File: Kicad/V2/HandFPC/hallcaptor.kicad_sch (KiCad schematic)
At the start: 0 parts

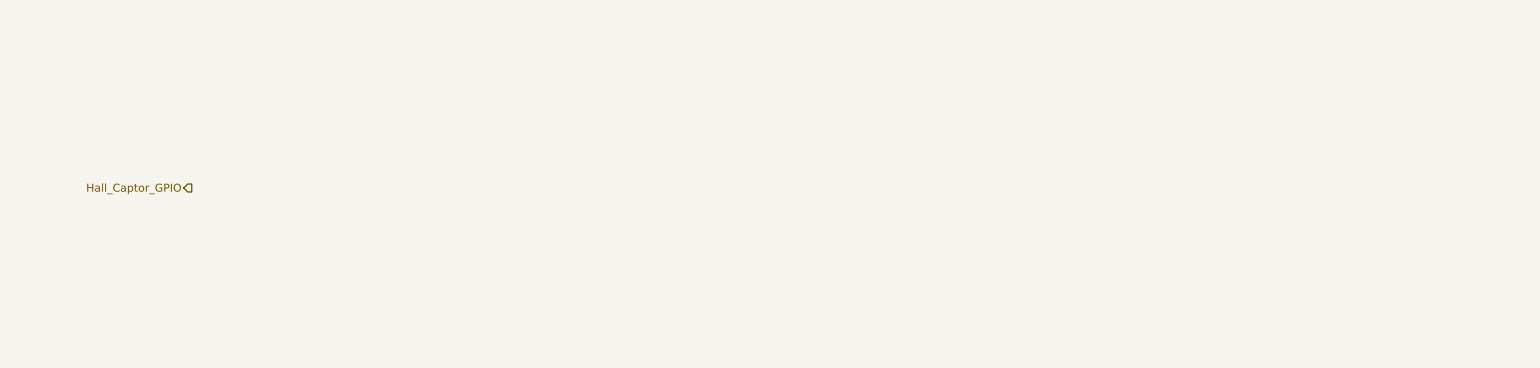
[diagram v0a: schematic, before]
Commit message: hand FPC pass erc no warning no error
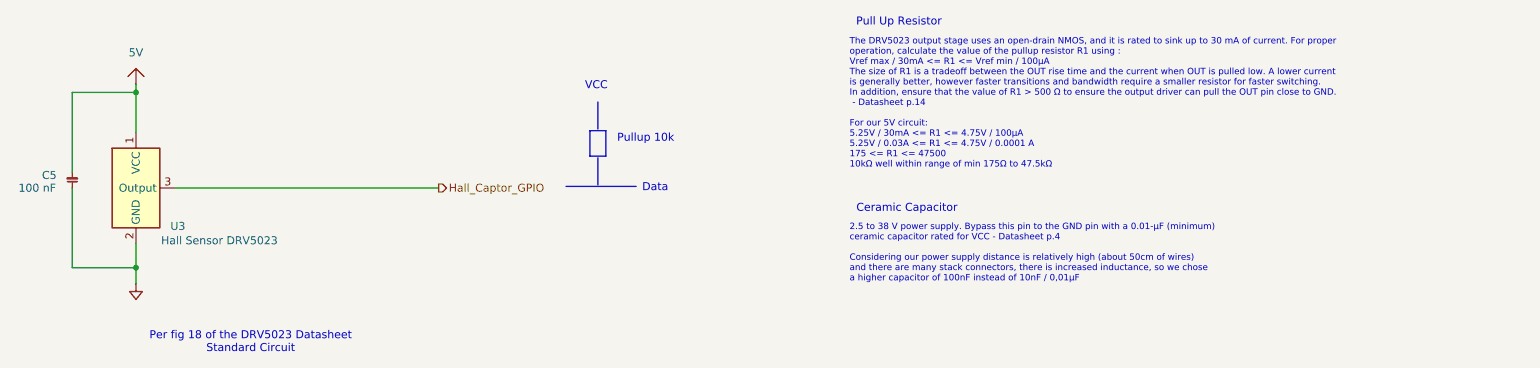
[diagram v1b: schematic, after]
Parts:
- added C5: 100 nF, symbol G-Love-Symbols:C
- added U3: Hall Sensor DRV5023, symbol G-Love-Symbols:DRV5023
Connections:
- net Hall_Captor_GPIO: now also U3.3 (Output)
- new net 5V: C5.1, U3.1 (VCC)
- new net GND: C5.2, U3.2 (GND)
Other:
- note added: "2.5 to 38 V power supply. Bypass this pin to the GND pin with a 0.01-μF (minimum) ceramic capacitor rated for VCC - Datasheet p.4 Considering our power supply distance is relatively high (about 50cm of wires) and there are many stack connectors, there is increased inductance, so we chose a higher capacitor of 100nF instead of 10nF / 0,01μF"
- note added: "Ceramic Capacitor"
- note added: "Data"
- note added: "Per fig 18 of the DRV5023 Datasheet Standard Circuit"
- note added: "Pull Up Resistor"
- note added: "Pullup 10k"
- note added: "The DRV5023 output stage uses an open-drain NMOS, and it is rated to sink up to 30 mA of current. For proper operation, calculate the value of the pullup resistor R1 using : Vref max / 30mA <= R1 <= Vref min / 100μA The size of R1 is a tradeoff between the OUT rise time and the current when OUT is pulled low. A lower current is generally better, however faster transitions and bandwidth require a 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"
- note added: "VCC"

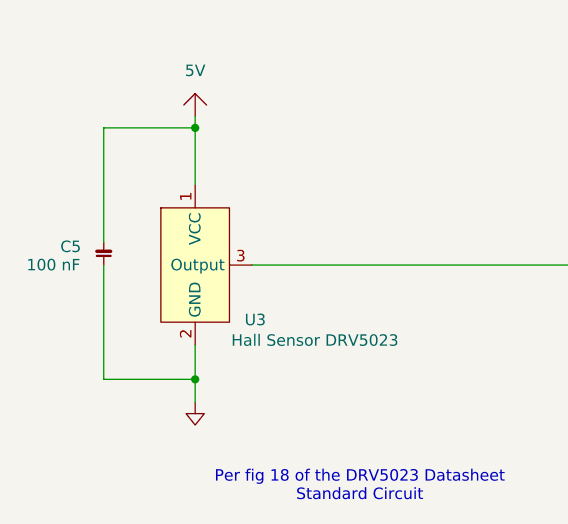
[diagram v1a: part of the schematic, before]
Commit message: add custom symbol for FPC connector
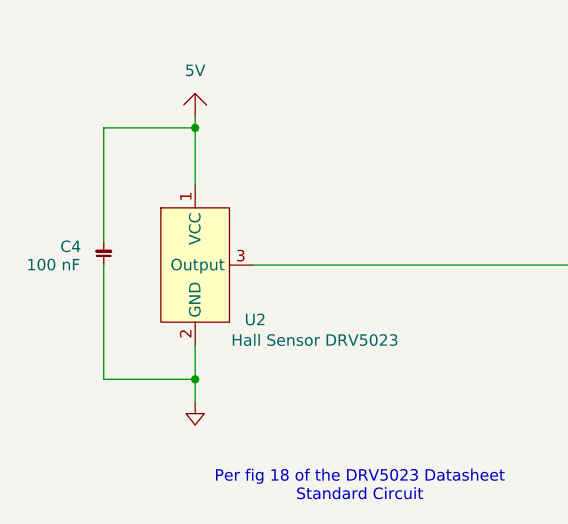
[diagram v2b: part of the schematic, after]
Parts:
- renumbered C5 to C4, U3 to U2
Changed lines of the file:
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@@
 		(dnp no)
 		(fields_autoplaced yes)
-		(property "Reference" "#PWR025"
+		(property "Reference" "#PWR024"
 			(at 50.8 27.3049 0)
 			(hide yes)
@@
 			(project "HandFPC"
 				(path "/7221f3d8-f3bc-4a50-a6fd-69c2d8ca27db/54aec40e-cdbe-47d9-8050-c74604c00f1a"
-					(reference "#PWR025")
+					(reference "#PWR024")
 					(unit 1)
 				)
@@
 		(in_pos_files yes)
 		(dnp no)
-		(property "Reference" "C5"
+		(property "Reference" "C4"
 			(at 33.274 44.958 0)
 			(show_name no)
@@
 			(project "HandFPC"
 				(path "/7221f3d8-f3bc-4a50-a6fd-69c2d8ca27db/54aec40e-cdbe-47d9-8050-c74604c00f1a"
-					(reference "C5")
+					(reference "C4")
 					(unit 1)
 				)
@@
 		(in_pos_files yes)
 		(dnp no)
-		(property "Reference" "U3"
+		(property "Reference" "U2"
 			(at 56.134 53.086 0)
 			(show_name no)
@@
 			(project "HandFPC"
 				(path "/7221f3d8-f3bc-4a50-a6fd-69c2d8ca27db/54aec40e-cdbe-47d9-8050-c74604c00f1a"
-					(reference "U3")
-					(unit 1)
-				)
+					(reference "U2")
+					(unit 1)
+				)

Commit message: fix flex sensor mixed up with force sensor
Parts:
- C4: footprint (none) -> MyGlove:Capacitor_0603
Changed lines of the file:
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@@
 			)
 		)
-		(property "Footprint" ""
+		(property "Footprint" "MyGlove:Capacitor_0603"
 			(at 38.1 45.72 0)
 			(hide yes)

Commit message: add FPC footprints
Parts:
- C4: footprint MyGlove:Capacitor_0603 -> MyGlove:FPC_0603
- U2: footprint (none) -> MyGlove:FPC_SOT_23
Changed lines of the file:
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@@
 			)
 		)
-		(property "Footprint" "MyGlove:Capacitor_0603"
+		(property "Footprint" "MyGlove:FPC_0603"
 			(at 38.1 45.72 0)
 			(hide yes)
@@
 			)
 		)
-		(property "Footprint" ""
+		(property "Footprint" "MyGlove:FPC_SOT_23"
 			(at 48.26 44.45 0)
 			(hide yes)

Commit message: add routing
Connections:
- net 5V renamed +3.3V
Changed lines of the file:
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@@
-	)
-	(symbol
-		(lib_id "G-Love-Symbols:+5V")
-		(at 48.26 27.94 0)
-		(unit 1)
-		(body_style 1)
-		(exclude_from_sim no)
-		(in_bom no)
-		(on_board no)
-		(in_pos_files yes)
-		(dnp no)
-		(fields_autoplaced yes)
-		(property "Reference" "#PWR024"
-			(at 50.8 27.3049 0)
-			(hide yes)
-			(show_name no)
-			(do_not_autoplace no)
-			(effects
-				(font
-					(size 1.27 1.27)
-				)
-				(justify left)
-			)
-		)
-		(property "Value" "5V"
-			(at 48.26 25.4 0)
-			(show_name no)
-			(do_not_autoplace no)
-			(effects
-				(font
-					(size 1.27 1.27)
-				)
-			)
-		)
-		(property "Footprint" ""
-			(at 48.26 27.94 0)
-			(hide yes)
-			(show_name no)
-			(do_not_autoplace no)
-			(effects
-				(font
-					(size 1.27 1.27)
-				)
-			)
-		)
-		(property "Datasheet" ""
-			(at 48.26 27.94 0)
-			(hide yes)
-			(show_name no)
-			(do_not_autoplace no)
-			(effects
-				(font
-					(size 1.27 1.27)
-				)
-			)
-		)
-		(property "Description" ""
-			(at 48.26 27.94 0)
-			(hide yes)
-			(show_name no)
-			(do_not_autoplace no)
-			(effects
-				(font
-					(size 1.27 1.27)
-				)
-			)
-		)
-		(pin "1"
-		)
-		(instances
-			(project "HandFPC"
-				(path "/7221f3d8-f3bc-4a50-a6fd-69c2d8ca27db/54aec40e-cdbe-47d9-8050-c74604c00f1a"
-					(reference "#PWR024")
-					(unit 1)
-				)
-			)
-		)
 	)
 	(symbol
@@
 					(unit 1)
 				)
+			)
+		)
+	)
+	(symbol
+		(lib_id "G-Love-Symbols:+3.3V")
+		(at 48.26 29.21 0)
+		(unit 1)
+		(body_style 1)
+		(exclude_from_sim no)
+		(in_bom no)
+		(on_board no)
+		(in_pos_files yes)
+		(dnp no)
+		(property "Reference" "#PWR022"
+			(at 52.07 30.988 0)
+			(hide yes)
+			(show_name no)
+			(do_not_autoplace no)
+			(effects
+				(font
+					(size 1.27 1.27)
+				)
+			)
+		)
+		(property "Value" "+3.3V"
+			(at 51.562 27.686 0)
+			(show_name no)
+			(do_not_autoplace no)
+			(effects
+				(font
+					(size 1.27 1.27)
+				)
+			)
+		)
+		(property "Footprint" ""
+			(at 48.26 29.21 0)
+			(hide yes)
+			(show_name no)
+			(do_not_autoplace no)
+			(effects
+				(font
+					(size 1.27 1.27)
+				)
+			)
+		)
+		(property "Datasheet" ""
+			(at 48.26 29.21 0)
+			(hide yes)
+			(show_name no)
+			(do_not_autoplace no)
+			(effects
+				(font
+					(size 1.27 1.27)
+				)
+			)
+		)
+		(property "Description" ""
+			(at 48.26 29.21 0)
+			(hide yes)
+			(show_name no)
+			(do_not_autoplace no)
+			(effects
+				(font
+					(size 1.27 1.27)
+				)
+			)
+		)
+		(pin "1"
+		)
+		(instances
+			(project "HandFPC"
+				(path "/7221f3d8-f3bc-4a50-a6fd-69c2d8ca27db/54aec40e-cdbe-47d9-8050-c74604c00f1a"
+					(reference "#PWR022")
+					(unit 1)
+				)
